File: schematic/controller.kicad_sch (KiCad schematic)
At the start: 2 parts, among them U18 74LS541, U19 74LS541

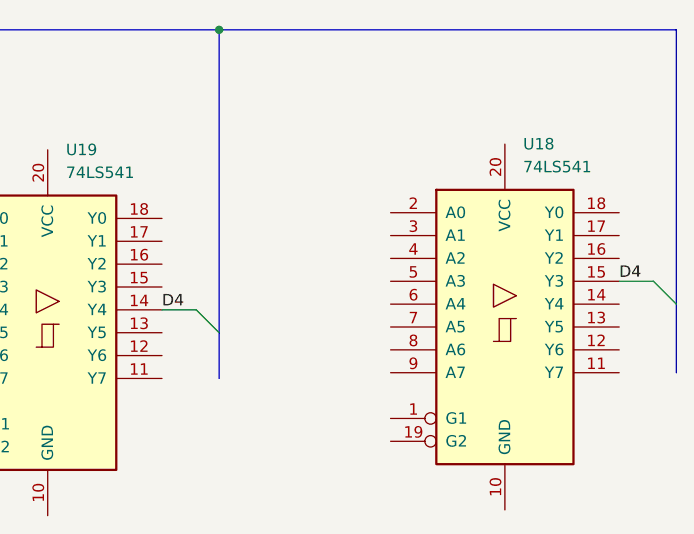
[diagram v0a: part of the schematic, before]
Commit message: worked on the z80 trace up to and including pin 15.
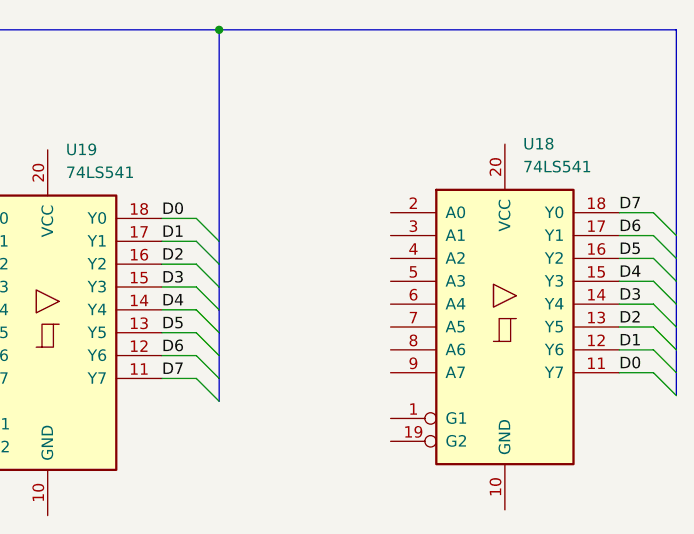
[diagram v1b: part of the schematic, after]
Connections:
- net D7: now reaches U19.11 (Y7)
- net D7: now also U18.18 (Y0)
- net D6: now reaches U19.12 (Y6)
- net D6: now also U18.17 (Y1)
- net D5: now reaches U19.13 (Y5)
- net D5: now also U18.16 (Y2)
- net D3: now reaches U19.15 (Y3)
- net D3: now also U18.14 (Y4)
- net D2: now reaches U19.16 (Y2)
- net D2: now also U18.13 (Y5)
- net D1: now reaches U19.17 (Y1)
- net D1: now also U18.12 (Y6)
- net D0: now reaches U19.18 (Y0)
- net D0: now also U18.11 (Y7)
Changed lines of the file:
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@@
   (junction (at 142.875 53.975) (diameter 0) (color 0 0 0 0)
   )
+  (bus_entry (at 140.335 77.47) (size 2.54 2.54)
+    (stroke (width 0) (type default) (color 0 0 0 0))
+  )
+  (bus_entry (at 140.335 92.71) (size 2.54 2.54)
+    (stroke (width 0) (type default) (color 0 0 0 0))
+  )
   (bus_entry (at 140.335 85.09) (size 2.54 2.54)
     (stroke (width 0) (type default) (color 0 0 0 0))
   )
+  (bus_entry (at 191.135 89.535) (size 2.54 2.54)
+    (stroke (width 0) (type default) (color 0 0 0 0))
+  )
+  (bus_entry (at 191.135 74.295) (size 2.54 2.54)
+    (stroke (width 0) (type default) (color 0 0 0 0))
+  )
+  (bus_entry (at 191.135 86.995) (size 2.54 2.54)
+    (stroke (width 0) (type default) (color 0 0 0 0))
+  )
+  (bus_entry (at 191.135 76.835) (size 2.54 2.54)
+    (stroke (width 0) (type default) (color 0 0 0 0))
+  )
+  (bus_entry (at 191.135 84.455) (size 2.54 2.54)
+    (stroke (width 0) (type default) (color 0 0 0 0))
+  )
+  (bus_entry (at 140.335 87.63) (size 2.54 2.54)
+    (stroke (width 0) (type default) (color 0 0 0 0))
+  )
+  (bus_entry (at 191.135 79.375) (size 2.54 2.54)
+    (stroke (width 0) (type default) (color 0 0 0 0))
+  )
   (bus_entry (at 191.135 81.915) (size 2.54 2.54)
     (stroke (width 0) (type default) (color 0 0 0 0))
   )
-  (bus (pts (xy 142.875 53.975) (xy 142.875 87.63))
+  (bus_entry (at 140.335 82.55) (size 2.54 2.54)
+    (stroke (width 0) (type default) (color 0 0 0 0))
+  )
+  (bus_entry (at 140.335 74.93) (size 2.54 2.54)
+    (stroke (width 0) (type default) (color 0 0 0 0))
+  )
+  (bus_entry (at 140.335 90.17) (size 2.54 2.54)
+    (stroke (width 0) (type default) (color 0 0 0 0))
+  )
+  (bus_entry (at 191.135 92.075) (size 2.54 2.54)
+    (stroke (width 0) (type default) (color 0 0 0 0))
+  )
+  (bus_entry (at 140.335 80.01) (size 2.54 2.54)
+    (stroke (width 0) (type default) (color 0 0 0 0))
+  )
+  (bus (pts (xy 142.875 77.47) (xy 142.875 80.01))
+    (stroke (width 0) (type default) (color 0 0 0 0))
+  )
+  (wire (pts (xy 187.325 79.375) (xy 191.135 79.375))
+    (stroke (width 0) (type default) (color 0 0 0 0))
+  )
+  (bus (pts (xy 142.875 53.975) (xy 142.875 77.47))
+    (stroke (width 0) (type default) (color 0 0 0 0))
+  )
+  (wire (pts (xy 136.525 82.55) (xy 140.335 82.55))
+    (stroke (width 0) (type default) (color 0 0 0 0))
+  )
+  (wire (pts (xy 136.525 87.63) (xy 140.335 87.63))
+    (stroke (width 0) (type default) (color 0 0 0 0))
+  )
+  (bus (pts (xy 142.875 80.01) (xy 142.875 82.55))
+    (stroke (width 0) (type default) (color 0 0 0 0))
+  )
+  (wire (pts (xy 136.525 74.93) (xy 140.335 74.93))
+    (stroke (width 0) (type default) (color 0 0 0 0))
+  )
+  (wire (pts (xy 187.325 84.455) (xy 191.135 84.455))
     (stroke (width 0) (type default) (color 0 0 0 0))
   )
@@
     (stroke (width 0) (type default) (color 0 0 0 0))
   )
+  (wire (pts (xy 187.325 92.075) (xy 191.135 92.075))
+    (stroke (width 0) (type default) (color 0 0 0 0))
+  )
+  (bus (pts (xy 193.675 81.915) (xy 193.675 84.455))
+    (stroke (width 0) (type default) (color 0 0 0 0))
+  )
+  (bus (pts (xy 142.875 90.17) (xy 142.875 92.71))
+    (stroke (width 0) (type default) (color 0 0 0 0))
+  )
+  (wire (pts (xy 136.525 92.71) (xy 140.335 92.71))
+    (stroke (width 0) (type default) (color 0 0 0 0))
+  )
+  (wire (pts (xy 187.325 86.995) (xy 191.135 86.995))
+    (stroke (width 0) (type default) (color 0 0 0 0))
+  )
+  (wire (pts (xy 187.325 76.835) (xy 191.135 76.835))
+    (stroke (width 0) (type default) (color 0 0 0 0))
+  )
+  (bus (pts (xy 142.875 85.09) (xy 142.875 87.63))
+    (stroke (width 0) (type default) (color 0 0 0 0))
+  )
+  (wire (pts (xy 187.325 74.295) (xy 191.135 74.295))
+    (stroke (width 0) (type default) (color 0 0 0 0))
+  )
+  (bus (pts (xy 193.675 76.835) (xy 193.675 79.375))
+    (stroke (width 0) (type default) (color 0 0 0 0))
+  )
+  (bus (pts (xy 193.675 92.075) (xy 193.675 94.615))
+    (stroke (width 0) (type default) (color 0 0 0 0))
+  )
   (bus (pts (xy 93.98 53.975) (xy 142.875 53.975))
     (stroke (width 0) (type default) (color 0 0 0 0))
   )
-  (bus (pts (xy 142.875 87.63) (xy 142.875 92.71))
+  (bus (pts (xy 142.875 87.63) (xy 142.875 90.17))
     (stroke (width 0) (type default) (color 0 0 0 0))
   )
@@
     (stroke (width 0) (type default) (color 0 0 0 0))
   )
-  (bus (pts (xy 193.675 53.975) (xy 193.675 84.455))
-    (stroke (width 0) (type default) (color 0 0 0 0))
-  )
-  (bus (pts (xy 193.675 84.455) (xy 193.675 92.075))
-    (stroke (width 0) (type default) (color 0 0 0 0))
+  (bus (pts (xy 193.675 53.975) (xy 193.675 76.835))
+    (stroke (width 0) (type default) (color 0 0 0 0))
+  )
+  (bus (pts (xy 193.675 79.375) (xy 193.675 81.915))
+    (stroke (width 0) (type default) (color 0 0 0 0))
+  )
+  (bus (pts (xy 193.675 84.455) (xy 193.675 86.995))
+    (stroke (width 0) (type default) (color 0 0 0 0))
+  )
+  (wire (pts (xy 136.525 77.47) (xy 140.335 77.47))
+    (stroke (width 0) (type default) (color 0 0 0 0))
+  )
+  (wire (pts (xy 136.525 80.01) (xy 140.335 80.01))
+    (stroke (width 0) (type default) (color 0 0 0 0))
+  )
+  (bus (pts (xy 142.875 82.55) (xy 142.875 85.09))
+    (stroke (width 0) (type default) (color 0 0 0 0))
+  )
+  (wire (pts (xy 136.525 90.17) (xy 140.335 90.17))
+    (stroke (width 0) (type default) (color 0 0 0 0))
+  )
+  (bus (pts (xy 193.675 86.995) (xy 193.675 89.535))
+    (stroke (width 0) (type default) (color 0 0 0 0))
+  )
+  (bus (pts (xy 142.875 92.71) (xy 142.875 95.25))
+    (stroke (width 0) (type default) (color 0 0 0 0))
+  )
+  (wire (pts (xy 187.325 89.535) (xy 191.135 89.535))
+    (stroke (width 0) (type default) (color 0 0 0 0))
+  )
+  (bus (pts (xy 193.675 89.535) (xy 193.675 92.075))
+    (stroke (width 0) (type default) (color 0 0 0 0))
+  )
+  (label "D7" (at 136.525 92.71 0)
+    (effects (font (size 1.27 1.27)) (justify left bottom))
+  )
+  (label "D6" (at 187.325 76.835 0)
+    (effects (font (size 1.27 1.27)) (justify left bottom))
+  )
+  (label "D5" (at 187.325 79.375 0)
+    (effects (font (size 1.27 1.27)) (justify left bottom))
+  )
+  (label "D7" (at 187.325 74.295 0)
+    (effects (font (size 1.27 1.27)) (justify left bottom))
+  )
+  (label "D5" (at 136.525 87.63 0)
+    (effects (font (size 1.27 1.27)) (justify left bottom))
   )
   (label "D4" (at 187.325 81.915 0)
     (effects (font (size 1.27 1.27)) (justify left bottom))
   )
+  (label "D0" (at 136.525 74.93 0)
+    (effects (font (size 1.27 1.27)) (justify left bottom))
+  )
+  (label "D1" (at 136.525 77.47 0)
+    (effects (font (size 1.27 1.27)) (justify left bottom))
+  )
   (label "D4" (at 136.525 85.09 0)
     (effects (font (size 1.27 1.27)) (justify left bottom))
   )
+  (label "D0" (at 187.325 92.075 0)
+    (effects (font (size 1.27 1.27)) (justify left bottom))
+  )
+  (label "D1" (at 187.325 89.535 0)
+    (effects (font (size 1.27 1.27)) (justify left bottom))
+  )
+  (label "D6" (at 136.525 90.17 0)
+    (effects (font (size 1.27 1.27)) (justify left bottom))
+  )
+  (label "D3" (at 136.525 82.55 0)
+    (effects (font (size 1.27 1.27)) (justify left bottom))
+  )
+  (label "D2" (at 187.325 86.995 0)
+    (effects (font (size 1.27 1.27)) (justify left bottom))
+  )
+  (label "D3" (at 187.325 84.455 0)
+    (effects (font (size 1.27 1.27)) (justify left bottom))
+  )
+  (label "D2" (at 136.525 80.01 0)
+    (effects (font (size 1.27 1.27)) (justify left bottom))
+  )

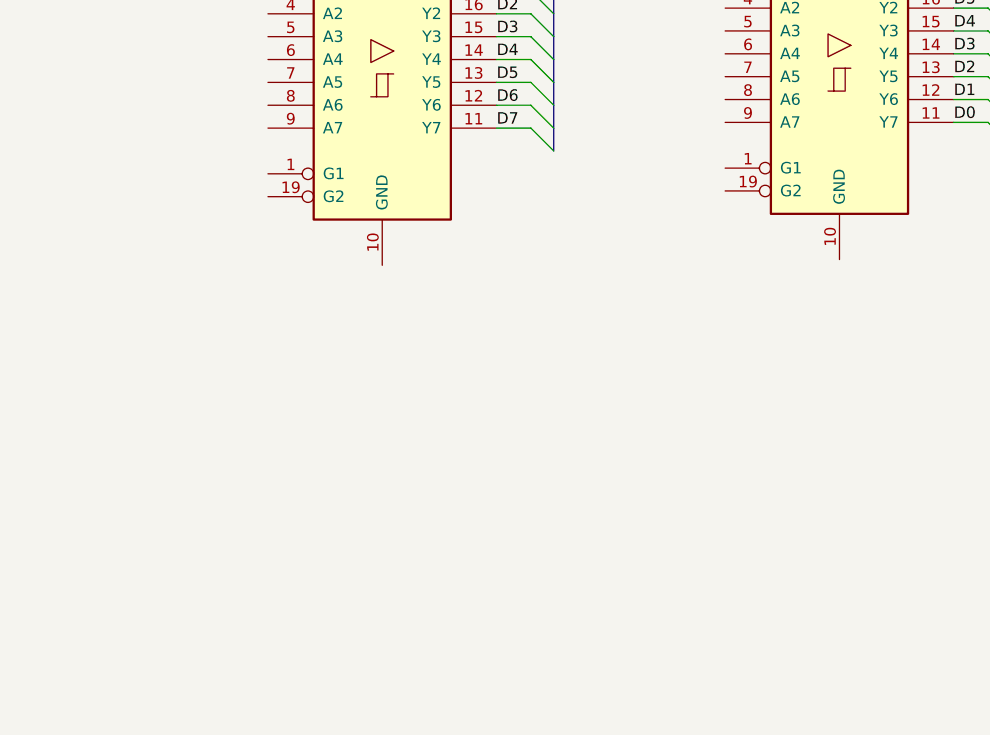
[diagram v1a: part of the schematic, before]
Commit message: added u6 decoder lines, renamed a few lines to make sense to there destination.
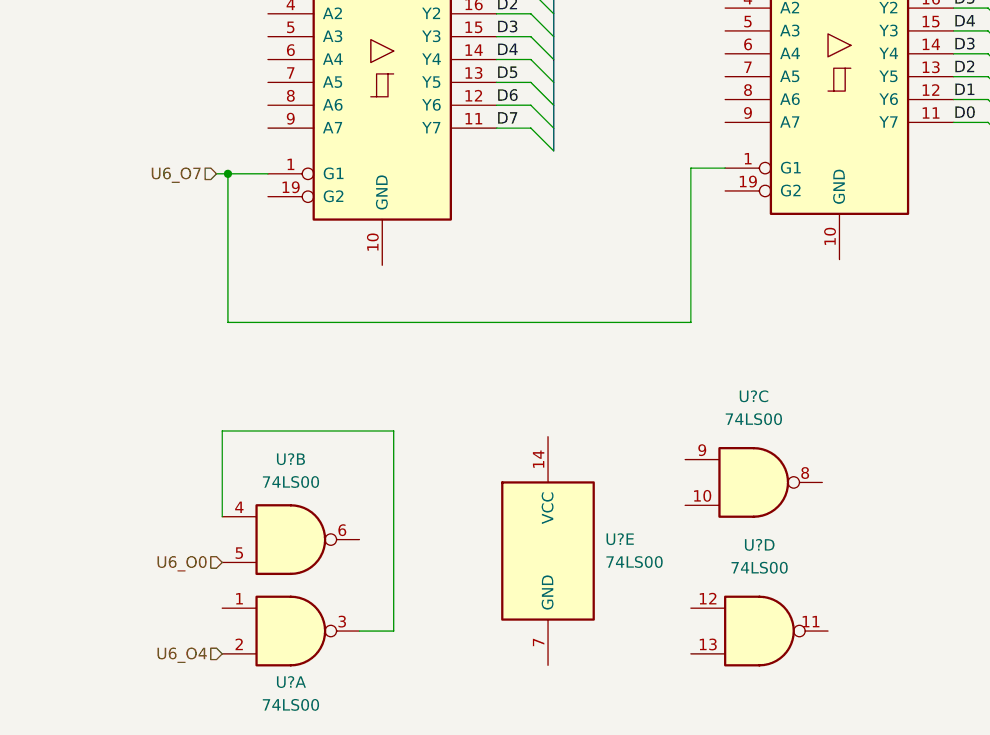
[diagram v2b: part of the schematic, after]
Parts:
- added U? (x5): 74LS00, symbol 74xx:74LS00
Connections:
- net U6_O7: now reaches U19.1 (G1)
- net U6_O7: now also U18.1 (G1)
- new net: U?.3, U?.4
- new net U6_O0: U?.5
- new net U6_O4: U?.2
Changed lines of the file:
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@@
 (kicad_sch (version 20211123) (generator eeschema)
   (paper "A4")
+  (junction (at 106.68 97.79) (diameter 0) (color 0 0 0 0)
+  )
   (junction (at 142.875 53.975) (diameter 0) (color 0 0 0 0)
   )
@@
     (stroke (width 0) (type default) (color 0 0 0 0))
   )
+  (wire (pts (xy 106.045 126.365) (xy 106.045 135.89))
+    (stroke (width 0) (type default) (color 0 0 0 0))
+  )
+  (wire (pts (xy 106.68 97.79) (xy 106.68 114.3))
+    (stroke (width 0) (type default) (color 0 0 0 0))
+  )
   (bus (pts (xy 142.875 53.975) (xy 142.875 77.47))
     (stroke (width 0) (type default) (color 0 0 0 0))
   )
+  (wire (pts (xy 106.68 97.79) (xy 111.125 97.79))
+    (stroke (width 0) (type default) (color 0 0 0 0))
+  )
   (wire (pts (xy 136.525 82.55) (xy 140.335 82.55))
     (stroke (width 0) (type default) (color 0 0 0 0))
@@
     (stroke (width 0) (type default) (color 0 0 0 0))
   )
+  (wire (pts (xy 106.68 114.3) (xy 158.115 114.3))
+    (stroke (width 0) (type default) (color 0 0 0 0))
+  )
   (wire (pts (xy 187.325 76.835) (xy 191.135 76.835))
     (stroke (width 0) (type default) (color 0 0 0 0))
@@
     (stroke (width 0) (type default) (color 0 0 0 0))
   )
+  (wire (pts (xy 158.115 97.155) (xy 161.925 97.155))
+    (stroke (width 0) (type default) (color 0 0 0 0))
+  )
   (wire (pts (xy 136.525 85.09) (xy 140.335 85.09))
     (stroke (width 0) (type default) (color 0 0 0 0))
@@
     (stroke (width 0) (type default) (color 0 0 0 0))
   )
+  (wire (pts (xy 105.41 97.79) (xy 106.68 97.79))
+    (stroke (width 0) (type default) (color 0 0 0 0))
+  )
   (bus (pts (xy 193.675 53.975) (xy 193.675 76.835))
     (stroke (width 0) (type default) (color 0 0 0 0))
@@
     (stroke (width 0) (type default) (color 0 0 0 0))
   )
+  (wire (pts (xy 125.095 126.365) (xy 125.095 148.59))
+    (stroke (width 0) (type default) (color 0 0 0 0))
+  )
+  (wire (pts (xy 121.285 148.59) (xy 125.095 148.59))
+    (stroke (width 0) (type default) (color 0 0 0 0))
+  )
   (bus (pts (xy 193.675 89.535) (xy 193.675 92.075))
     (stroke (width 0) (type default) (color 0 0 0 0))
   )
+  (wire (pts (xy 125.095 126.365) (xy 106.045 126.365))
+    (stroke (width 0) (type default) (color 0 0 0 0))
+  )
+  (wire (pts (xy 158.115 114.3) (xy 158.115 97.155))
+    (stroke (width 0) (type default) (color 0 0 0 0))
+  )
   (label "D7" (at 136.525 92.71 0)
     (effects (font (size 1.27 1.27)) (justify left bottom))
@@
   (label "D2" (at 136.525 80.01 0)
     (effects (font (size 1.27 1.27)) (justify left bottom))
+  )
+  (hierarchical_label "U6_O0" (shape input) (at 106.045 140.97 180)
+    (effects (font (size 1.27 1.27)) (justify right))
+  )
+  (hierarchical_label "U6_O4" (shape input) (at 106.045 151.13 180)
+    (effects (font (size 1.27 1.27)) (justify right))
+  )
+  (hierarchical_label "U6_O7" (shape input) (at 105.41 97.79 180)
+    (effects (font (size 1.27 1.27)) (justify right))
   )
   (hierarchical_label "D[0..7]" (shape bidirectional) (at 93.98 53.975 180)
@@
     (pin "9")
   )
+  (symbol (lib_id "74xx:74LS00") (at 165.735 148.59 0) (unit 4)
+    (in_bom yes) (on_board yes) (fields_autoplaced)
+    (property "Reference" "U?" (id 0) (at 165.735 139.065 0))
+    (property "Value" "74LS00" (id 1) (at 165.735 141.605 0))
+    (property "Footprint" "" (id 2) (at 165.735 148.59 0)
+      (effects (font (size 1.27 1.27)) hide)
+    )
+    (property "Datasheet" "http://www.ti.com/lit/gpn/sn74ls00" (id 3) (at 165.735 148.59 0)
+      (effects (font (size 1.27 1.27)) hide)
+    )
+    (pin "1")
+    (pin "2")
+    (pin "3")
+    (pin "4")
+    (pin "5")
+    (pin "6")
+    (pin "10")
+    (pin "8")
+    (pin "9")
+    (pin "11")
+    (pin "12")
+    (pin "13")
+    (pin "14")
+    (pin "7")
+  )
   (symbol (lib_id "74xx:74LS541") (at 174.625 86.995 0) (unit 1)
     (in_bom yes) (on_board yes) (fields_autoplaced)
@@
     (pin "9")
   )
+  (symbol (lib_id "74xx:74LS00") (at 142.24 139.7 0) (unit 5)
+    (in_bom yes) (on_board yes) (fields_autoplaced)
+    (property "Reference" "U?" (id 0) (at 148.59 138.4299 0)
+      (effects (font (size 1.27 1.27)) (justify left))
+    )
+    (property "Value" "74LS00" (id 1) (at 148.59 140.9699 0)
+      (effects (font (size 1.27 1.27)) (justify left))
+    )
+    (property "Footprint" "" (id 2) (at 142.24 139.7 0)
+      (effects (font (size 1.27 1.27)) hide)
+    )
+    (property "Datasheet" "http://www.ti.com/lit/gpn/sn74ls00" (id 3) (at 142.24 139.7 0)
+      (effects (font (size 1.27 1.27)) hide)
+    )
+    (pin "1")
+    (pin "2")
+    (pin "3")
+    (pin "4")
+    (pin "5")
+    (pin "6")
+    (pin "10")
+    (pin "8")
+    (pin "9")
+    (pin "11")
+    (pin "12")
+    (pin "13")
+    (pin "14")
+    (pin "7")
+  )
+  (symbol (lib_id "74xx:74LS00") (at 165.1 132.08 0) (unit 3)
+    (in_bom yes) (on_board yes) (fields_autoplaced)
+    (property "Reference" "U?" (id 0) (at 165.1 122.555 0))
+    (property "Value" "74LS00" (id 1) (at 165.1 125.095 0))
+    (property "Footprint" "" (id 2) (at 165.1 132.08 0)
+      (effects (font (size 1.27 1.27)) hide)
+    )
+    (property "Datasheet" "http://www.ti.com/lit/gpn/sn74ls00" (id 3) (at 165.1 132.08 0)
+      (effects (font (size 1.27 1.27)) hide)
+    )
+    (pin "1")
+    (pin "2")
+    (pin "3")
+    (pin "4")
+    (pin "5")
+    (pin "6")
+    (pin "10")
+    (pin "8")
+    (pin "9")
+    (pin "11")
+    (pin "12")
+    (pin "13")
+    (pin "14")
+    (pin "7")
+  )
+  (symbol (lib_id "74xx:74LS00") (at 113.665 148.59 0) (unit 1)
+    (in_bom yes) (on_board yes)
+    (property "Reference" "U?" (id 0) (at 113.665 154.305 0))
+    (property "Value" "74LS00" (id 1) (at 113.665 156.845 0))
+    (property "Footprint" "" (id 2) (at 113.665 148.59 0)
+      (effects (font (size 1.27 1.27)) hide)
+    )
+    (property "Datasheet" "http://www.ti.com/lit/gpn/sn74ls00" (id 3) (at 113.665 148.59 0)
+      (effects (font (size 1.27 1.27)) hide)
+    )
+    (pin "1")
+    (pin "2")
+    (pin "3")
+    (pin "4")
+    (pin "5")
+    (pin "6")
+    (pin "10")
+    (pin "8")
+    (pin "9")
+    (pin "11")
+    (pin "12")
+    (pin "13")
+    (pin "14")
+    (pin "7")
+  )
+  (symbol (lib_id "74xx:74LS00") (at 113.665 138.43 0) (unit 2)
+    (in_bom yes) (on_board yes) (fields_autoplaced)
+    (property "Reference" "U?" (id 0) (at 113.665 129.54 0))
+    (property "Value" "74LS00" (id 1) (at 113.665 132.08 0))
+    (property "Footprint" "" (id 2) (at 113.665 138.43 0)
+      (effects (font (size 1.27 1.27)) hide)
+    )
+    (property "Datasheet" "http://www.ti.com/lit/gpn/sn74ls00" (id 3) (at 113.665 138.43 0)
+      (effects (font (size 1.27 1.27)) hide)
+    )
+    (pin "1")
+    (pin "2")
+    (pin "3")
+    (pin "4")
+    (pin "5")
+    (pin "6")
+    (pin "10")
+    (pin "8")
+    (pin "9")
+    (pin "11")
+    (pin "12")
+    (pin "13")
+    (pin "14")
+    (pin "7")
+  )
 )
